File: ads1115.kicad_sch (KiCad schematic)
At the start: 15 parts, among them J31 Conn_01x05, J32 Conn_01x03, J33 Conn_01x03, J34 Conn_01x03, J35 Conn_01x03, U20 ADS1115IDGS

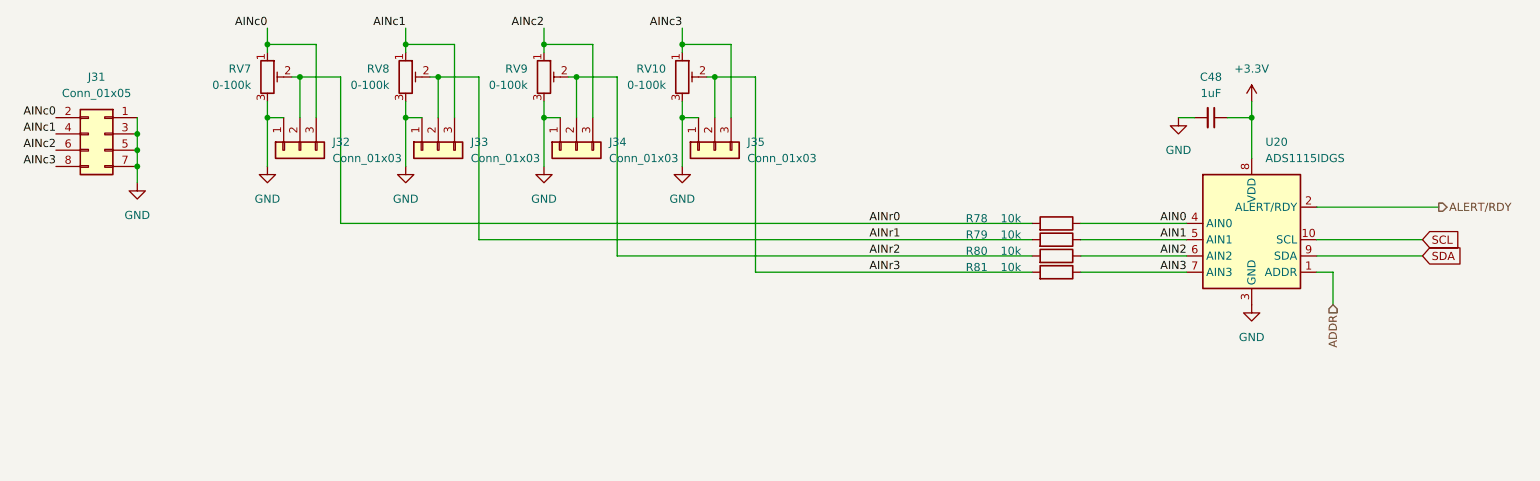
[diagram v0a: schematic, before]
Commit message: Update the design to a stackable one
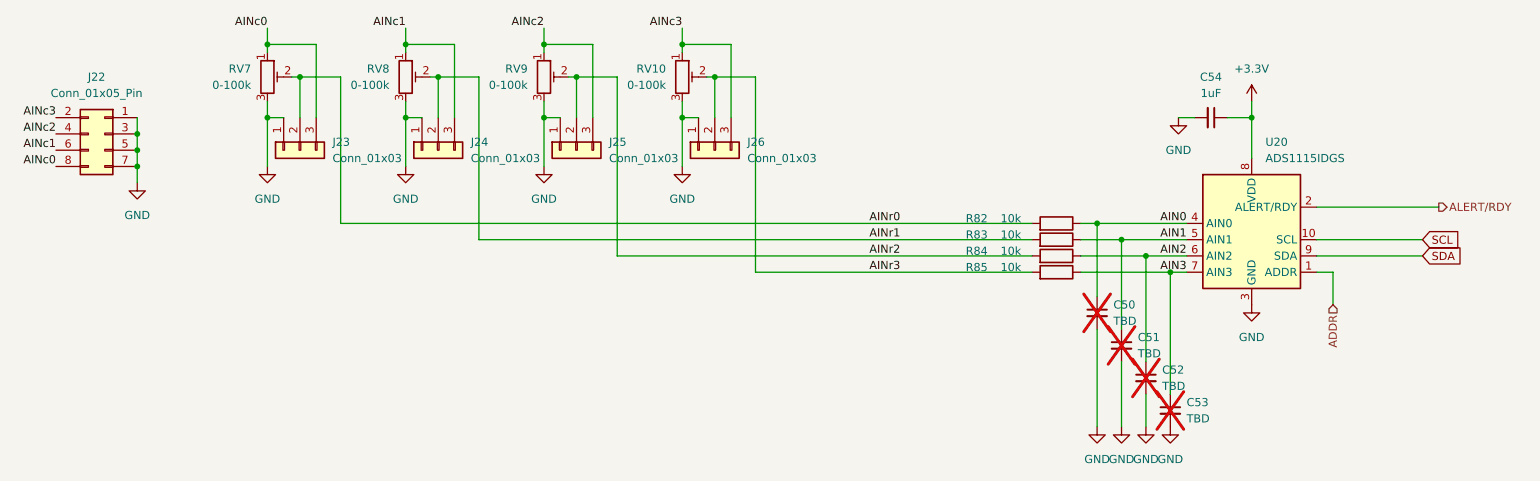
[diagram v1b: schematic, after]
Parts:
- added C50, C51, C52, C53: TBD, Capacitor_SMD:C_0603_1608Metric, symbol Device:C_Small
- J22: renamed from J31; value Conn_01x05 -> Conn_01x05_Pin; JLCPCB_CORRECTION 0;5.08;270 -> 1.27;-3.81;270; LCSC C492404 -> C492421
- renumbered C48 to C54, J32 to J23, J33 to J24, J34 to J25, J35 to J26, R78 to R82, R79 to R83, R80 to R84, R81 to R85
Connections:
- net AIN0: now also C50.1
- net AIN1: now also C51.1
- net AIN2: now also C52.1
- net AIN3: now also C53.1
- net AINc0: now also J22.8 (Pin_8); no longer J22.2 (Pin_2)
- net AINc1: now also J22.6 (Pin_6); no longer J22.4 (Pin_4)
- net AINc2: now also J22.4 (Pin_4); no longer J22.6 (Pin_6)
- net AINc3: now also J22.2 (Pin_2); no longer J22.8 (Pin_8)
- net GND: now also C50.2, C51.2, C52.2, C53.2
